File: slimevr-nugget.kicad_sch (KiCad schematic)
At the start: 56 parts, among them U1 nRF52840-QFXX, U3 XC6220B331MR, U4 LSM6DSV, U5 1532H, U6 QMC6309, U7 BQ24073RGT, Y1 32MHz

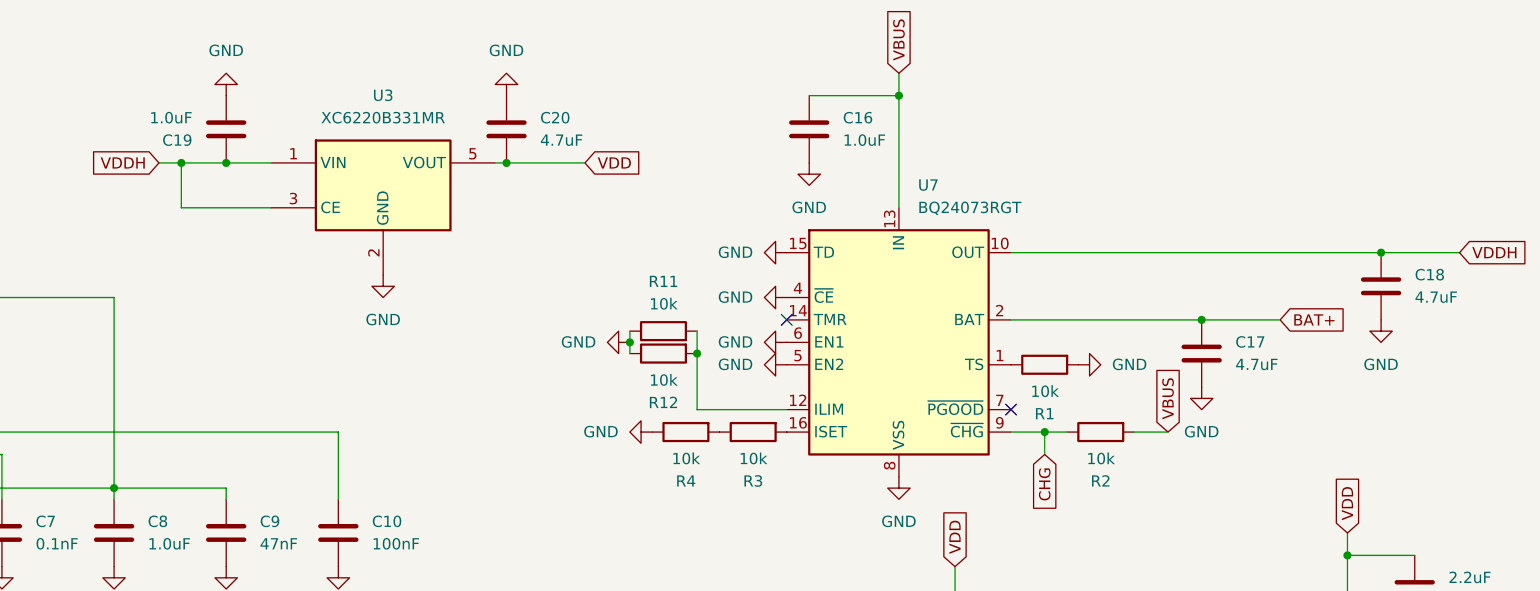
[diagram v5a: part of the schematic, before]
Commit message: Turn off system by pulling down CE of LDO while charging
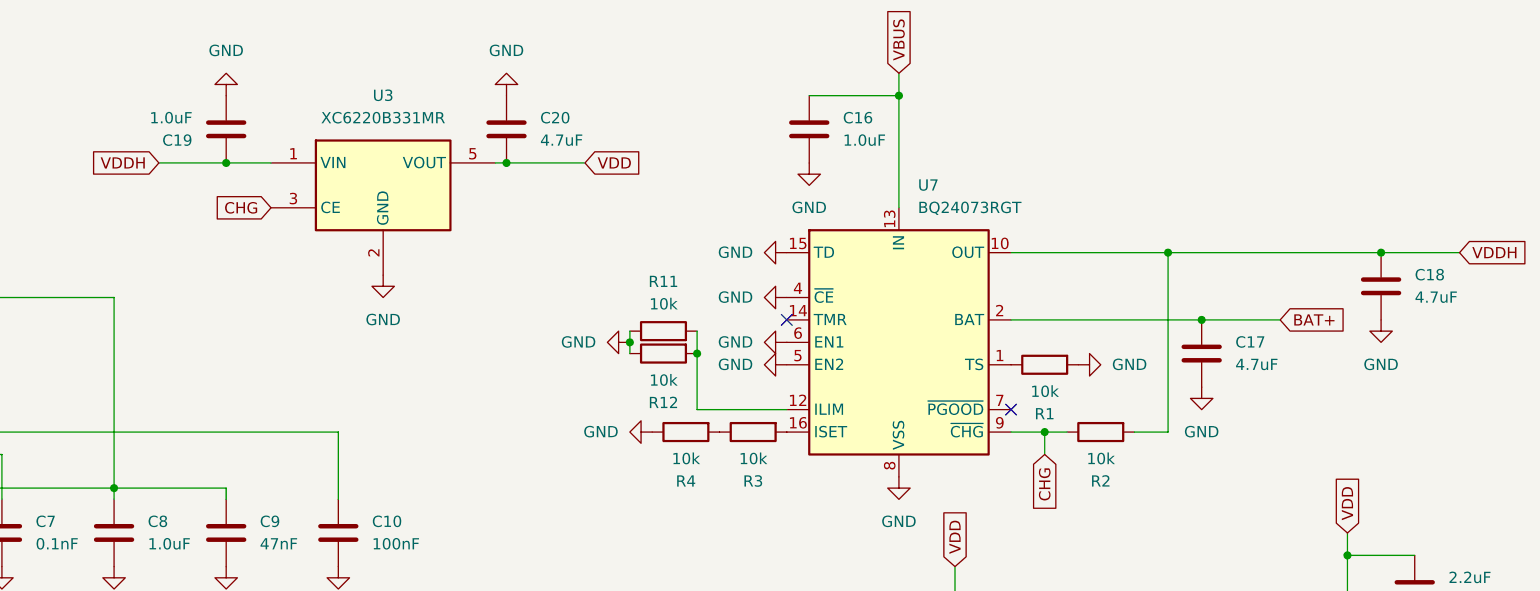
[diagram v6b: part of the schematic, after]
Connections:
- net CHG: now also U3.3 (CE)
- net VBUS: no longer R2.2
- net VDDH: now also R2.2; no longer U3.3 (CE)
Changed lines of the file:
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@@
+	)
+	(junction
+		(at 242.57 43.18)
+		(diameter 0)
+		(color 0 0 0 0)
 	)
 	(junction
@@
 	)
 	(junction
-		(at 130.81 33.02)
-		(diameter 0)
-		(color 0 0 0 0)
-	)
-	(junction
 		(at 266.7 43.18)
 		(diameter 0)
@@
 	(wire
 		(pts
-			(xy 130.81 33.02) (xy 135.89 33.02)
+			(xy 128.27 33.02) (xy 135.89 33.02)
 		)
 		(stroke
@@
 	(wire
 		(pts
-			(xy 224.79 43.18) (xy 266.7 43.18)
+			(xy 224.79 43.18) (xy 242.57 43.18)
 		)
 		(stroke
@@
 	(wire
 		(pts
-			(xy 130.81 38.1) (xy 140.97 38.1)
-		)
-		(stroke
-			(width 0)
-			(type default)
-		)
-	)
-	(wire
-		(pts
 			(xy 231.14 63.5) (xy 228.6 63.5)
 		)
@@
 	(wire
 		(pts
-			(xy 128.27 33.02) (xy 130.81 33.02)
-		)
-		(stroke
-			(width 0)
-			(type default)
-		)
-	)
-	(wire
-		(pts
 			(xy 113.03 109.22) (xy 110.49 109.22)
 		)
@@
 	(wire
 		(pts
+			(xy 242.57 43.18) (xy 242.57 63.5)
+		)
+		(stroke
+			(width 0)
+			(type default)
+		)
+	)
+	(wire
+		(pts
 			(xy 262.89 74.93) (xy 262.89 77.47)
 		)
@@
 	(wire
 		(pts
-			(xy 130.81 33.02) (xy 130.81 38.1)
-		)
-		(stroke
-			(width 0)
-			(type default)
-		)
-	)
-	(wire
-		(pts
 			(xy 41.91 30.48) (xy 41.91 27.94)
 		)
@@
 	(wire
 		(pts
+			(xy 242.57 43.18) (xy 266.7 43.18)
+		)
+		(stroke
+			(width 0)
+			(type default)
+		)
+	)
+	(wire
+		(pts
 			(xy 41.91 64.77) (xy 41.91 68.58)
 		)
@@
 		)
 	)
+	(global_label "CHG"
+		(shape input)
+		(at 140.97 38.1 180)
+		(fields_autoplaced yes)
+		(effects
+			(font
+				(size 1.27 1.27)
+			)
+			(justify right)
+		)
+		(property "Intersheetrefs" "${INTERSHEET_REFS}"
+			(at 134.1143 38.1 0)
+			(hide yes)
+			(show_name no)
+			(do_not_autoplace no)
+			(effects
+				(font
+					(size 1.27 1.27)
+				)
+				(justify right)
+			)
+		)
+	)
 	(global_label "VDD"
 		(shape input)
@@
 			(hide yes)
 			(show_name no)
-			(do_not_autoplace no)
-			(effects
-				(font
-					(size 1.27 1.27)
-				)
-				(justify left)
-			)
-		)
-	)
-	(global_label "VBUS"
-		(shape input)
-		(at 242.57 63.5 90)
-		(fields_autoplaced yes)
-		(effects
-			(font
-				(size 1.27 1.27)
-			)
-			(justify left)
-		)
-		(property "Intersheetrefs" "${INTERSHEET_REFS}"
-			(at 242.57 55.6162 90)
-			(hide yes)
-			(show_name no)

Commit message: Final production version
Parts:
- added D1, D2: LED, LED_SMD:LED_0402_1005Metric, symbol Device:LED
- added R13: 10k, Resistor_SMD:R_0402_1005Metric, symbol Device:R
- added R14: 1k, Resistor_SMD:R_0402_1005Metric, symbol Device:R
- R2: value 10k -> 1k
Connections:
- net CHG: now also R13.2; no longer R2.1, U7.9 (~{CHG})
- net GND: now also D2.1 (K)
- net VDDH: now also R13.1
- net at U1.13 (P0.13): now also R14.2
- new net: D1.1 (K), U7.9 (~{CHG})
- new net: D2.2 (A), R14.1
- new net: D1.2 (A), R2.1
- no-connect marks 29 -> 28
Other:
- moved on the sheet: C19, C20, C21, C22, C24, C3, R1, R10, R2, R5, R6, R7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

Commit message: Add 1:1 battery sensing circuit
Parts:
- added R15, R16: 100k, Resistor_SMD:R_0402_1005Metric, symbol Device:R
- R13: value 10k -> 100k
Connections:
- net BAT+: now also R16.2
- net GND: now also R15.1
- net BSENSE: now reaches U1.4 (P0.04)
- net BSENSE: now also R15.2, R16.1
- no-connect marks 28 -> 27
